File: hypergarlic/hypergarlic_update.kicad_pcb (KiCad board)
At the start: 2 copper layers, 238.8 x 87.7 mm, 40 parts, among them J1 AudioJack4dpb, J2 AudioJack4dpb, SW10 SW_Push, SW11 SW_Push, SW11_r1 SW_Push, SW12 SW_Push, SW12_r1 SW_Push, SW13_r1 SW_Push, SW14 SW_Push, SW15 SW_Push, SW15_r1 SW_Push, SW16 SW_Push, SW16_r1 SW_Push, SW17 SW_Push, SW17_r1 SW_Push, SW18 SW_Push, SW18_r1 SW_Push, SW2 SW_Push, SW20 SW_Push, SW20_r1 SW_Push, SW21 SW_Push, SW21_r1 SW_Push, SW2_r1 SW_Push, SW3 SW_Push, SW3_r1 SW_Push, SW4 SW_Push, SW4_r1 SW_Push, SW5 SW_Push, SW5_r1 SW_Push, SW6 SW_Push, SW6_r1 SW_Push, SW7_r1 SW_Push, SW8 SW_Push, SW8_r1 SW_Push, SW9 SW_Push, SW9_r1 SW_Push, U1 ProMicro-kbd, U2 ProMicro-kbd

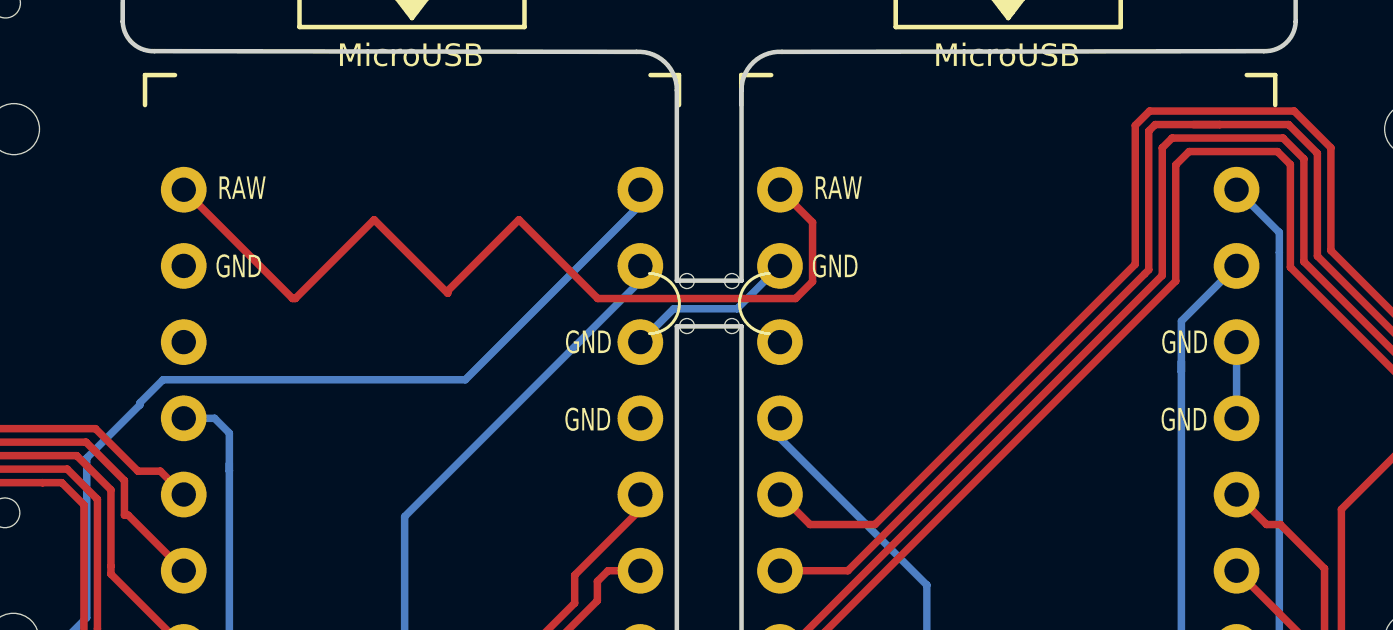
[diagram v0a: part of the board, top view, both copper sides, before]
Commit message: Archive old PCB, update circuits
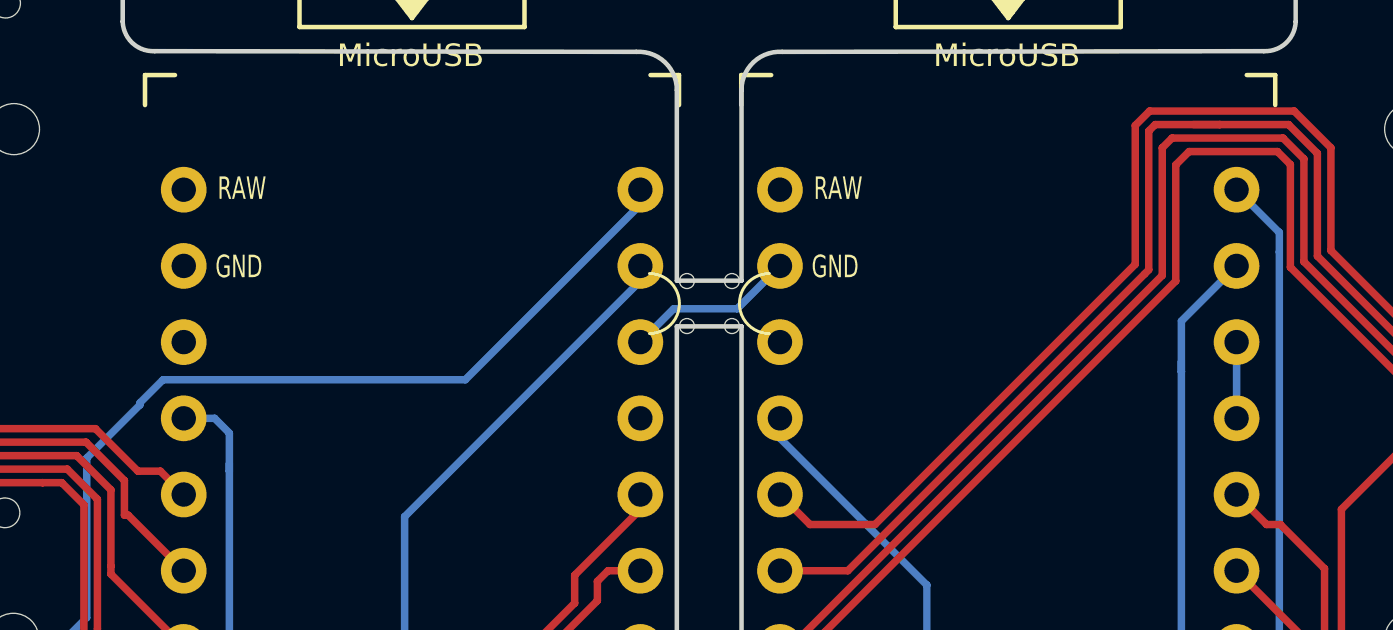
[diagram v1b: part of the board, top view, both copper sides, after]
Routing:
- net raw: track 30.5 -> 0.00 mm

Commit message: Minor trace changes
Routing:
- net vcc: track 85.7 -> 69.7 mm
- net Switch9: track 35.5 -> 34.2 mm
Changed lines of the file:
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@@
     (thickness 1.6)
     (drawings 52)
-    (tracks 695)
+    (tracks 688)
     (zones 0)
     (modules 40)
@@
   (gr_arc (start 61.491282 233.935279) (end 58.783546 110.725903) (angle 13.02135768) (layer Edge.Cuts) (width 0.15))
   (gr_arc (start 97.125046 113.418186) (end 96.774 115.062) (angle -17.50894085) (layer Edge.Cuts) (width 0.15))
-  (gr_text "Face down" (at 139.446 67.31 90) (layer F.SilkS)
+  (gr_text "Face down" (at 144.71 59.25 90) (layer F.SilkS)
     (effects (font (size 1.5 1.5) (thickness 0.3)))
   )
-  (gr_text "Face down" (at 119.888 66.294 90) (layer F.SilkS)
+  (gr_text "Face down" (at 124.81 59.25 90) (layer F.SilkS)
     (effects (font (size 1.5 1.5) (thickness 0.3)))
   )
@@
   (segment (start 140.868 78.218) (end 140.984 78.218) (width 0.25) (layer B.Cu) (net 2))
   (segment (start 141.868 59.4226) (end 141.868 77.334) (width 0.25) (layer B.Cu) (net 2))
-  (segment (start 130.288 82.818) (end 128.372 82.818) (width 0.25) (layer F.Cu) (net 2))
-  (segment (start 140.36 81.382) (end 131.724 81.382) (width 0.25) (layer F.Cu) (net 2))
-  (segment (start 131.724 81.382) (end 130.288 82.818) (width 0.25) (layer F.Cu) (net 2))
-  (segment (start 140.868 80.874) (end 140.36 81.382) (width 0.25) (layer F.Cu) (net 2))
-  (segment (start 140.868 78.218) (end 140.868 80.874) (width 0.25) (layer F.Cu) (net 2))
   (segment (start 124.706 82.152) (end 125.372 82.818) (width 0.25) (layer B.Cu) (net 3))
   (segment (start 124.46 82.152) (end 124.706 82.152) (width 0.25) (layer B.Cu) (net 3))
@@
   (segment (start 90.732599 63.683009) (end 97.67402 70.62443) (width 0.25) (layer F.Cu) (net 13))
   (segment (start 97.67402 70.62443) (end 99.3816 72.33201) (width 0.25) (layer F.Cu) (net 13))
-  (segment (start 109.728 72.39) (end 110.998 72.39) (width 0.25) (layer F.Cu) (net 13))
-  (segment (start 109.67001 72.33201) (end 109.728 72.39) (width 0.25) (layer F.Cu) (net 13))
   (segment (start 99.3816 72.33201) (end 109.53199 72.33201) (width 0.25) (layer F.Cu) (net 13))
   (segment (start 109.53199 72.33201) (end 109.67001 72.33201) (width 0.25) (layer F.Cu) (net 13))

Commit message: More trace corrections
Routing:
- net Switch7: track 81.8 -> 79.7 mm
